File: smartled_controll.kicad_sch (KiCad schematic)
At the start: 70 parts, among them J1 Conn_01x04, SW1 SW_Push, U1 OC5028B, U2 MAX485E, U3 PY32F003F1xUx, U4 OC5864, U5 need chooice, U7 need chooice, Y1 Crystal_GND23

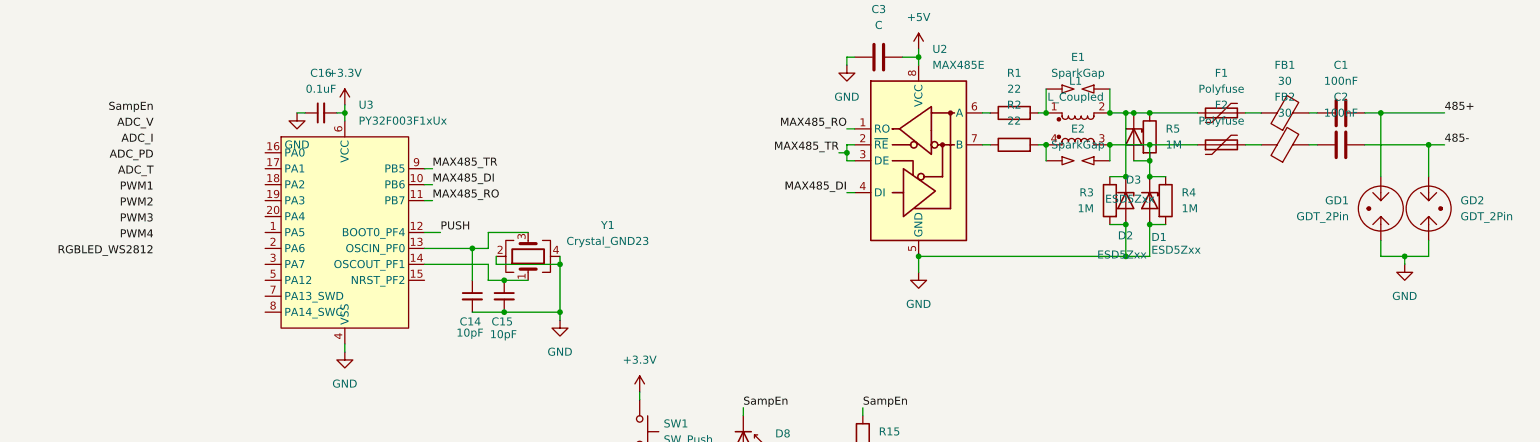
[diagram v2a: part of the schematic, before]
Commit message: 布线和调整布局，把PCB上的电路按模块分组
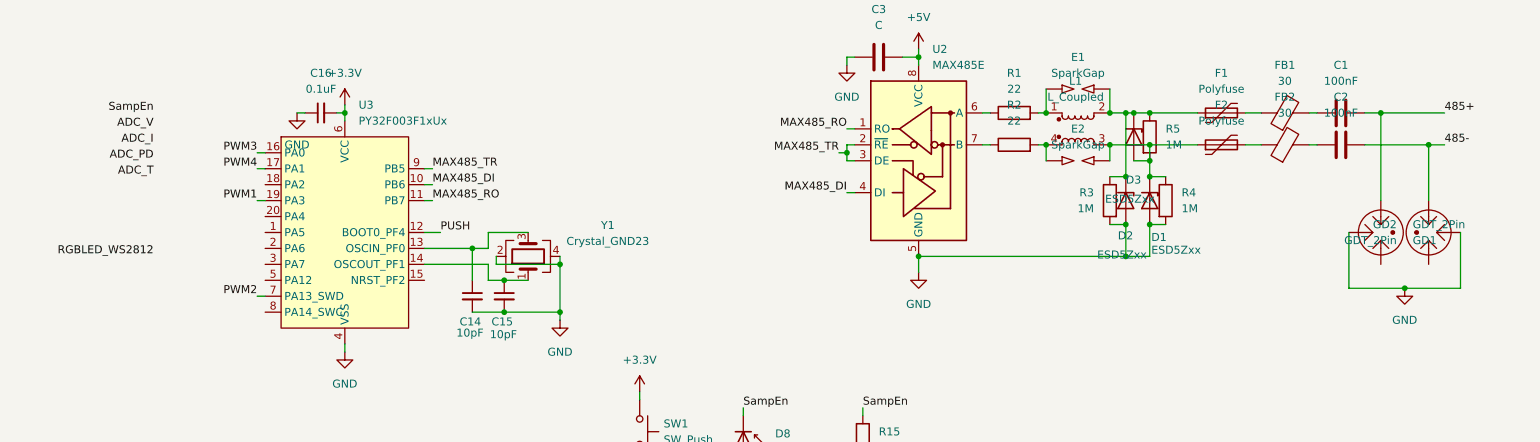
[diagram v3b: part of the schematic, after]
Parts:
- GD1, GD2: symbol Device:GDT_2Pin -> Device:GDT_3Pin
- R6, R7: footprint Resistor_SMD:R_0603_1608Metric -> Resistor_SMD:R_0402_1005Metric
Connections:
- net 485+: now also GD1.1; no longer GD1.3
- net 485-: now also GD2.1; no longer GD2.3
- net GND: now also GD1.2, GD2.2; no longer GD1.1, GD2.1
- net PWM1: now also U3.19 (PA3)
- net PWM2: now also U3.7 (PA13_SWD)
- net PWM3: now also U3.16 (PA0)
- net PWM4: now also U3.17 (PA1)
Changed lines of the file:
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@@
 	)
 	(junction
-		(at 250.19 102.87)
-		(diameter 0)
-		(color 0 0 0 0)
-	)
-	(junction
 		(at 80.01 29.21)
 		(diameter 0)
@@
 	)
 	(junction
+		(at 250.19 107.95)
+		(diameter 0)
+		(color 0 0 0 0)
+	)
+	(junction
 		(at 85.09 153.67)
 		(diameter 0)
@@
 	(wire
 		(pts
+			(xy 67.31 88.9) (xy 68.58 88.9)
+		)
+		(stroke
+			(width 0)
+			(type default)
+		)
+	)
+	(wire
+		(pts
 			(xy 81.28 78.74) (xy 81.28 80.01)
 		)
@@
 	(wire
 		(pts
-			(xy 246.38 80.01) (xy 246.38 90.17)
-		)
-		(stroke
-			(width 0)
-			(type default)
-		)
-	)
-	(wire
-		(pts
-			(xy 246.38 100.33) (xy 246.38 102.87)
+			(xy 246.38 80.01) (xy 246.38 93.98)
 		)
 		(stroke
@@
 	(wire
 		(pts
-			(xy 195.58 41.91) (xy 195.58 38.1)
+			(xy 259.08 99.06) (xy 259.08 107.95)
 		)
 		(stroke
@@
 	(wire
 		(pts
-			(xy 55.88 49.53) (xy 55.88 52.07)
-		)
-		(stroke
-			(width 0)
-			(type default)
-		)
-	)
-	(wire
-		(pts
-			(xy 144.78 137.16) (xy 149.86 137.16)
+			(xy 195.58 41.91) (xy 195.58 38.1)
 		)
 		(stroke
@@
 	(wire
 		(pts
-			(xy 205.74 50.8) (xy 205.74 52.07)
+			(xy 55.88 49.53) (xy 55.88 52.07)
 		)
 		(stroke
@@
 	(wire
 		(pts
-			(xy 254 102.87) (xy 250.19 102.87)
+			(xy 144.78 137.16) (xy 149.86 137.16)
 		)
 		(stroke
@@
 	(wire
 		(pts
-			(xy 246.38 102.87) (xy 250.19 102.87)
+			(xy 205.74 50.8) (xy 205.74 52.07)
 		)
 		(stroke
@@
 	(wire
 		(pts
+			(xy 241.3 107.95) (xy 250.19 107.95)
+		)
+		(stroke
+			(width 0)
+			(type default)
+		)
+	)
+	(wire
+		(pts
 			(xy 209.55 102.87) (xy 205.74 102.87)
 		)
@@
 	(wire
 		(pts
+			(xy 241.3 99.06) (xy 241.3 107.95)
+		)
+		(stroke
+			(width 0)
+			(type default)
+		)
+	)
+	(wire
+		(pts
+			(xy 67.31 86.36) (xy 68.58 86.36)
+		)
+		(stroke
+			(width 0)
+			(type default)
+		)
+	)
+	(wire
+		(pts
 			(xy 209.55 90.17) (xy 212.09 90.17)
 		)
@@
 	(wire
 		(pts
+			(xy 259.08 107.95) (xy 250.19 107.95)
+		)
+		(stroke
+			(width 0)
+			(type default)
+		)
+	)
+	(wire
+		(pts
 			(xy 217.17 85.09) (xy 209.55 85.09)
 		)
@@
 	(wire
 		(pts
+			(xy 67.31 93.98) (xy 68.58 93.98)
+		)
+		(stroke
+			(width 0)
+			(type default)
+		)
+	)
+	(wire
+		(pts
 			(xy 104.14 99.06) (xy 104.14 101.6)
 		)
@@
 	(wire
 		(pts
-			(xy 203.2 80.01) (xy 205.74 80.01)
+			(xy 67.31 109.22) (xy 68.58 109.22)
 		)
 		(stroke
@@
 	(wire
 		(pts
-			(xy 163.83 135.89) (xy 163.83 137.16)
+			(xy 203.2 80.01) (xy 205.74 80.01)
 		)
 		(stroke
@@
 	(wire
 		(pts
-			(xy 95.25 35.56) (xy 95.25 29.21)
+			(xy 163.83 135.89) (xy 163.83 137.16)
 		)
 		(stroke
@@
 	(wire
 		(pts
-			(xy 234.95 85.09) (xy 236.22 85.09)
+			(xy 95.25 35.56) (xy 95.25 29.21)
 		)
 		(stroke
@@
 	(wire
 		(pts
-			(xy 254 100.33) (xy 254 102.87)
+			(xy 234.95 85.09) (xy 236.22 85.09)
 		)
 		(stroke
@@
 	(wire
 		(pts
-			(xy 254 85.09) (xy 254 90.17)
+			(xy 254 85.09) (xy 254 93.98)
 		)
 		(stroke
@@
 	(wire
 		(pts
-			(xy 250.19 102.87) (xy 250.19 104.14)
-		)
-		(stroke
-			(width 0)
-			(type default)
-		)
-	)
-	(wire
-		(pts
 			(xy 218.44 41.91) (xy 218.44 39.37)
 		)
@@
 	)
 	(label "PWM1"
-		(at 50.8 92.71 180)
+		(at 67.31 93.98 180)
 		(effects
 			(font
@@
 	)
 	(label "PWM2"
-		(at 50.8 95.25 180)
+		(at 67.31 109.22 180)
 		(effects
 			(font
@@
 	)
 	(label "PWM3"
-		(at 50.8 97.79 180)
+		(at 67.31 86.36 180)
 		(effects
 			(font
@@
 	)
 	(label "PWM4"
-		(at 50.8 100.33 180)
+		(at 67.31 88.9 180)
 		(effects
 			(font
@@
 	(symbol
 		(lib_id "power:GND")
-		(at 250.19 104.14 0)
+		(at 250.19 107.95 0)
 		(unit 1)
 		(exclude_from_sim no)
@@
 		(fields_autoplaced yes)
 		(property "Reference" "#PWR09"
-			(at 250.19 110.49 0)
+			(at 250.19 114.3 0)
 			(effects
 				(font
@@
 		)
 		(property "Value" "GND"
-			(at 250.19 109.22 0)
+			(at 250.19 113.03 0)
 			(effects
 				(font
@@
 		)
 		(property "Footprint" ""
-			(at 250.19 104.14 0)
+			(at 250.19 107.95 0)
 			(effects
 				(font
@@
 		)
 		(property "Datasheet" ""
-			(at 250.19 104.14 0)
+			(at 250.19 107.95 0)
 			(effects
 				(font
@@
 		)
 		(property "Description" "Power symbol creates a global label with name \"GND\" , ground"
-			(at 250.19 104.14 0)
+			(at 250.19 107.95 0)
 			(effects
 				(font
@@
 			)
 		)
-		(property "Footprint" "Resistor_SMD:R_0603_1608Metric"
+		(property "Footprint" "Resistor_SMD:R_0402_1005Metric"
 			(at 198.12 44.958 90)
 			(effects
@@
 	)
 	(symbol
-		(lib_id "Device:GDT_2Pin")
-		(at 246.38 95.25 0)
-		(mirror y)
+		(lib_id "Device:GDT_3Pin")
+		(at 246.38 99.06 0)
+		(mirror x)
 		(unit 1)
 		(exclude_from_sim no)
@@
 		(dnp no)
 		(property "Reference" "GD1"
-			(at 241.3 93.9799 0)
+			(at 251.46 100.3301 0)
 			(effects
 				(font
@@
 		)
 		(property "Value" "GDT_2Pin"
-			(at 241.3 96.5199 0)
+			(at 251.46 97.7901 0)
 			(effects
 				(font
@@
 		)
 		(property "Footprint" "Capacitor_SMD:C_1812_4532Metric"
-			(at 246.38 95.25 90)
+			(at 246.38 99.06 90)
 			(effects
 				(font
@@
 		)
 		(property "Datasheet" "~"
-			(at 246.38 95.25 90)
+			(at 246.38 99.06 90)
 			(effects
 				(font
@@
 			)
 		)
-		(property "Description" "Gas Discharge Tube with 2 Pins"
-			(at 246.38 95.25 0)
+		(property "Description" "Gas Discharge Tube with 3 Pins"
+			(at 246.38 99.06 0)
 			(effects
 				(font
@@
 		(pin "3"
 		)
+		(pin "2"
+		)
 		(instances
 			(project ""
@@
 			)
 		)
-		(property "Footprint" "Resistor_SMD:R_0603_1608Metric"
+		(property "Footprint" "Resistor_SMD:R_0402_1005Metric"
 			(at 191.262 48.26 90)
 			(effects
@@
 	)
 	(symbol
-		(lib_id "Device:GDT_2Pin")
-		(at 254 95.25 0)
+		(lib_id "Device:GDT_3Pin")
+		(at 254 99.06 180)
 		(unit 1)
 		(exclude_from_sim no)
@@
 		(fields_autoplaced yes)
 		(property "Reference" "GD2"
-			(at 259.08 93.9799 0)
+			(at 248.92 97.7899 0)
 			(effects
 				(font
@@
 		)
 		(property "Value" "GDT_2Pin"
-			(at 259.08 96.5199 0)
+			(at 248.92 100.3299 0)
 			(effects
 				(font
@@
 		)
 		(property "Footprint" "Capacitor_SMD:C_1812_4532Metric"
-			(at 254 95.25 90)
+			(at 254 99.06 90)
 			(effects
 				(font
@@
 		)
 		(property "Datasheet" "~"
-			(at 254 95.25 90)
+			(at 254 99.06 90)
 			(effects
 				(font
@@
 			)
 		)
-		(property "Description" "Gas Discharge Tube with 2 Pins"
-			(at 254 95.25 0)
+		(property "Description" "Gas Discharge Tube with 3 Pins"
+			(at 254 99.06 0)
 			(effects
 				(font
@@
 		(pin "3"
 		)
+		(pin "2"
+		)
 		(instances

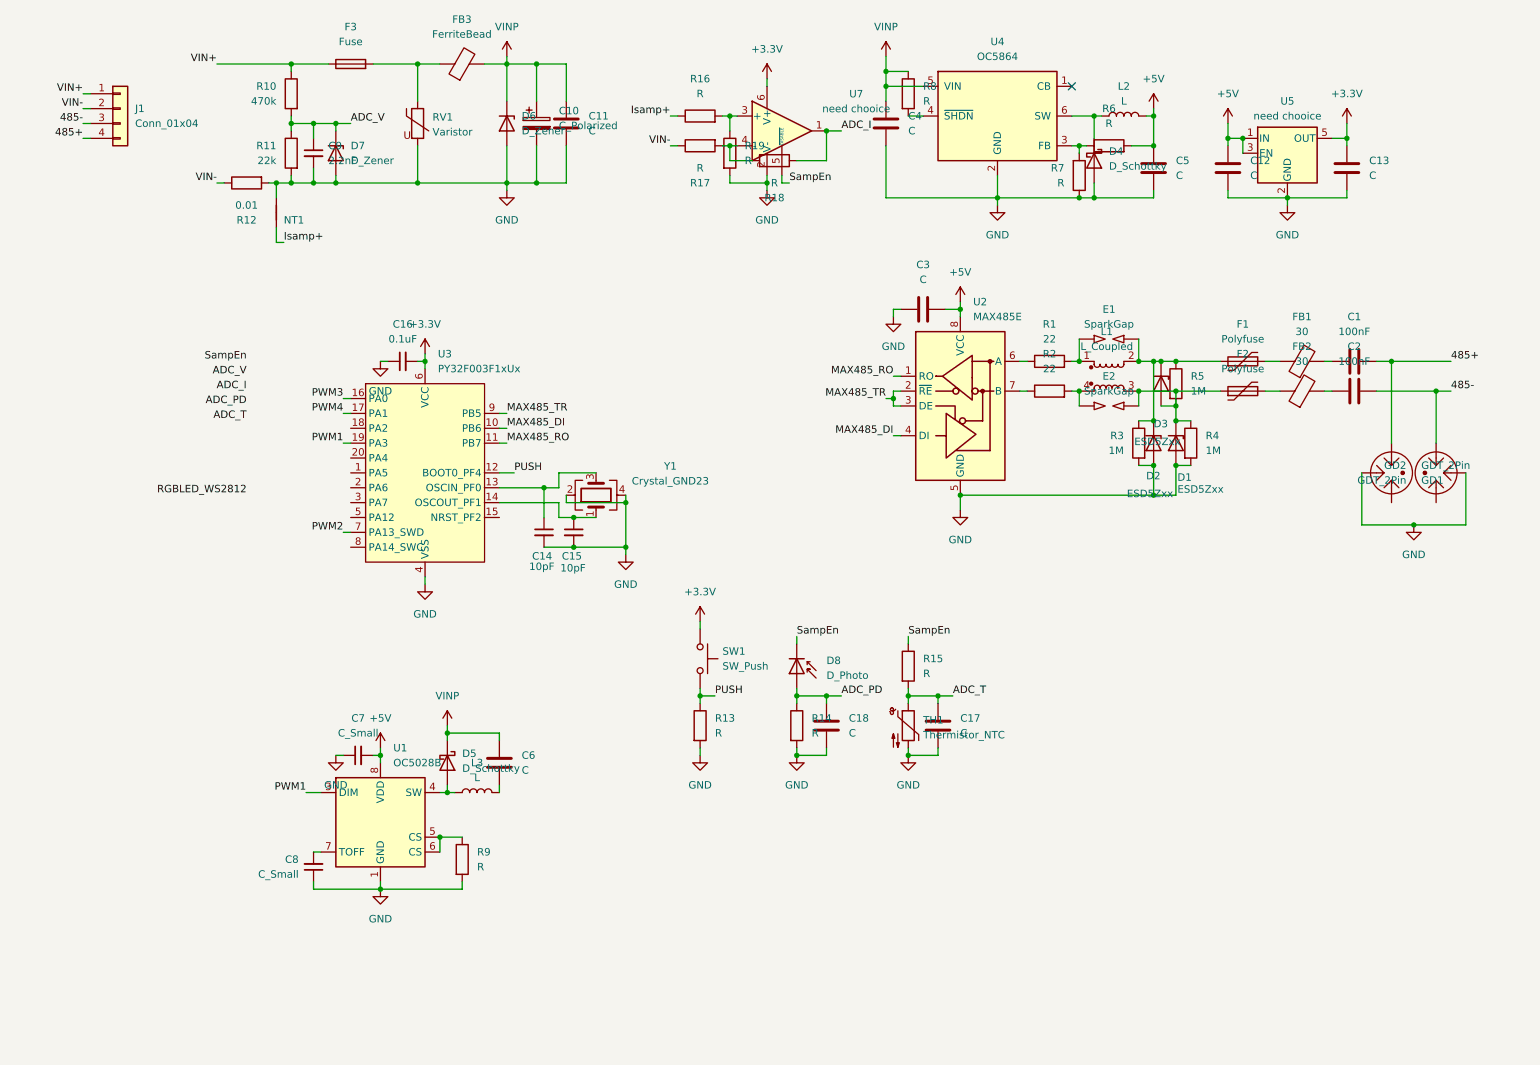
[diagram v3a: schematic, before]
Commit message: 复制LED驱动模块为4个
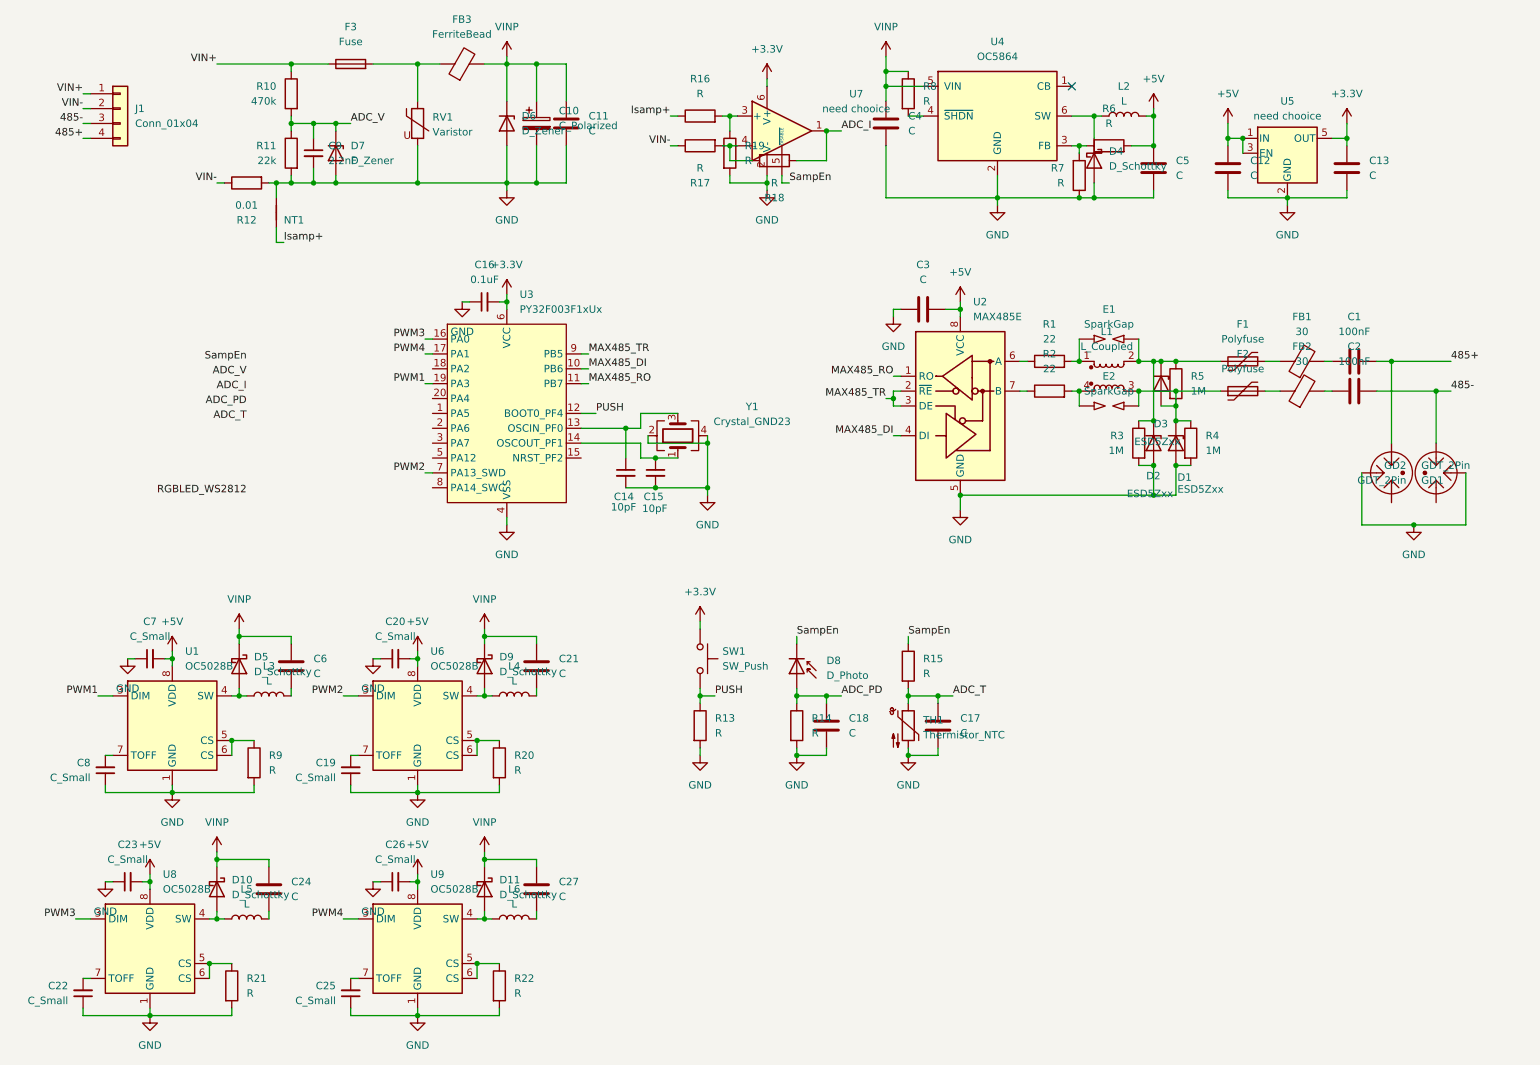
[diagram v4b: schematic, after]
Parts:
- added C19, C20, C22, C23, C25, C26: C_Small, Capacitor_SMD:C_0402_1005Metric, symbol Device:C_Small
- added C21, C24, C27: C, Capacitor_SMD:C_1210_3225Metric, symbol Device:C
- added D10, D11, D9: D_Schottky, Diode_SMD:D_SMA, symbol Device:D_Schottky
- added L4, L5, L6: L, Inductor_SMD:L_APV_APH0630, symbol Device:L
- added R20, R21, R22: R, Resistor_SMD:R_1206_3216Metric, symbol Device:R
- added U6, U8, U9: OC5028B, Package_SO:HSOP-8-1EP_3.9x4.9mm_P1.27mm_EP2.41x3.1mm_ThermalVias, symbol project_syms:OC5028B
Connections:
- net +5V: now also C20.2, C23.2, C26.2, U6.8 (VDD), U8.8 (VDD), U9.8 (VDD)
- net GND: now also C19.1, C20.1, C22.1, C23.1, C25.1, C26.1, R20.2, R21.2, R22.2, U6.1 (GND), U6.2 (NC), U6.9 (GND), U8.1 (GND), U8.2 (NC), U8.9 (GND), U9.1 (GND), U9.2 (NC), U9.9 (GND)
- net PWM2: now also U6.3 (DIM)
- net PWM3: now also U8.3 (DIM)
- net PWM4: now also U9.3 (DIM)
- net VINP: now also C21.1, C24.1, C27.1, D10.1 (K), D11.1 (K), D9.1 (K)
- new net: D9.2 (A), L4.1, U6.4 (SW)
- new net: C27.2, L6.2
- new net: D10.2 (A), L5.1, U8.4 (SW)
- new net: C24.2, L5.2
- new net: C19.2, U6.7 (TOFF)
- new net: C21.2, L4.2
- new net: D11.2 (A), L6.1, U9.4 (SW)
- new net: R22.1, U9.5 (CS), U9.6 (CS)
- new net: C25.2, U9.7 (TOFF)
- new net: R20.1, U6.5 (CS), U6.6 (CS)
- new net: R21.1, U8.5 (CS), U8.6 (CS)
- new net: C22.2, U8.7 (TOFF)
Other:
- moved on the sheet: C14, C15, C16, C6, C7, C8, D5, L3, R9, U1, U3, Y1

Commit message: 布线和微调布局（除光电二极管和温度传感器外）
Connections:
- net ADC_I: now also U3.2 (PA6)
- net ADC_V: now also U3.3 (PA7)
- net PWM1: now also U3.16 (PA0); no longer U3.19 (PA3)
- net PWM3: now also U3.19 (PA3); no longer U3.16 (PA0)
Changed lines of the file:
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@@
+	(wire
+		(pts
+			(xy 81.28 93.98) (xy 82.55 93.98)
+		)
+		(stroke
+			(width 0)
+			(type default)
+		)
+	)
 	(wire
 		(pts
@@
 		(pts
 			(xy 90.17 175.26) (xy 91.44 175.26)
+		)
+		(stroke
+			(width 0)
+			(type default)
+		)
+	)
+	(wire
+		(pts
+			(xy 81.28 91.44) (xy 82.55 91.44)
 		)
 		(stroke
@@
 		)
 	)
-	(label "PWM1"
-		(at 81.28 83.82 180)
-		(effects
-			(font
-				(size 1.27 1.27)
-			)
-			(justify right bottom)
-		)
-	)
 	(label "MAX485_RO"
 		(at 161.29 82.55 180)
@@
 	)
 	(label "ADC_V"
-		(at 50.8 82.55 180)
+		(at 81.28 93.98 180)
 		(effects
 			(font
@@
 		)
 	)
-	(label "PWM3"
-		(at 81.28 76.2 180)
-		(effects
-			(font
-				(size 1.27 1.27)
-			)
-			(justify right bottom)
-		)
-	)
 	(label "RGBLED_WS2812"
 		(at 50.8 102.87 180)
@@
 		)
 	)
+	(label "PWM1"
+		(at 81.28 76.2 180)
+		(effects
+			(font
+				(size 1.27 1.27)
+			)
+			(justify right bottom)
+		)
+	)
 	(label "SampEn"
 		(at 50.8 80.01 180)
@@
 		)
 	)
+	(label "PWM3"
+		(at 81.3449 83.82 180)
+		(effects
+			(font
+				(size 1.27 1.27)
+			)
+			(justify right bottom)
+		)
+	)
 	(label "ADC_I"
-		(at 50.8 85.09 180)
-		(effects
-			(font
+		(at 81.28 91.44 180)
+		(effects
+			(font

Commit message: 调整布局，划出PCB边框，MCU连接光电二极管和温度传感器
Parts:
- D8: footprint Connector_PinHeader_1.00mm:PinHeader_1x02_P1.00mm_Vertical -> Diode_SMD:D_0805_2012Metric
- TH1: footprint Connector_PinHeader_1.00mm:PinHeader_1x02_P1.00mm_Vertical -> Resistor_SMD:R_0805_2012Metric
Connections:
- net ADC_PD: now also U3.1 (PA5)
- net ADC_T: now also U3.18 (PA2)
- net SampEn: now also U3.20 (PA4)
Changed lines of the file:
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@@
 	(wire
 		(pts
+			(xy 81.28 88.9) (xy 82.55 88.9)
+		)
+		(stroke
+			(width 0)
+			(type default)
+		)
+	)
+	(wire
+		(pts
 			(xy 193.04 85.09) (xy 193.04 87.63)
 		)
@@
 	(wire
 		(pts
+			(xy 81.28 86.36) (xy 82.55 86.36)
+		)
+		(stroke
+			(width 0)
+			(type default)
+		)
+	)
+	(wire
+		(pts
 			(xy 128.27 137.16) (xy 130.81 137.16)
 		)
@@
 	(wire
 		(pts
+			(xy 81.28 81.28) (xy 82.55 81.28)
+		)
+		(stroke
+			(width 0)
+			(type default)
+		)
+	)
+	(wire
+		(pts
 			(xy 80.01 29.21) (xy 80.01 35.56)
 		)
@@
 	)
 	(label "ADC_PD"
-		(at 50.8 87.63 180)
+		(at 81.28 88.9 180)
 		(effects
 			(font
@@
 	)
 	(label "ADC_T"
-		(at 50.8 90.17 180)
+		(at 81.28 81.28 180)
 		(effects
 			(font
@@
 	)
 	(label "SampEn"
-		(at 50.8 80.01 180)
+		(at 81.28 86.36 180)
 		(effects
 			(font
@@
 	)
 	(label "PWM3"
-		(at 81.3449 83.82 180)
+		(at 81.28 83.82 180)
 		(effects
 			(font
@@
 			)
 		)
-		(property "Footprint" "Connector_PinHeader_1.00mm:PinHeader_1x02_P1.00mm_Vertical"
+		(property "Footprint" "Diode_SMD:D_0805_2012Metric"
 			(at 144.78 132.08 0)
 			(effects
@@
 			)
 		)
-		(property "Footprint" "Connector_PinHeader_1.00mm:PinHeader_1x02_P1.00mm_Vertical"
+		(property "Footprint" "Resistor_SMD:R_0805_2012Metric"
 			(at 163.83 140.97 0)
 			(effects
